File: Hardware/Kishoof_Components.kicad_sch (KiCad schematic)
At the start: 54 parts, among them J1 SWD_Header, J2 Eurorack_10_pin_power, U1 STM32H7B0VBTx, U2 PCM5100APW, U3 TPS561201, U4 LT1117-3.3, U5 TL074, U6 MX25LM51245G, Y1 8MHz 20pF

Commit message: Additional schematic layout
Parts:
- added C33, C34: 100nF, Capacitor_SMD:C_0603_1608Metric_Pad1.08x0.95mm_HandSolder, symbol Device:C_Small
- added C35: 1.5nF, Capacitors_SMD:C_0603_HandSoldering, symbol Device:C_Small
- added C36: 100nF, Capacitor_SMD:C_0603_1608Metric, symbol Device:C_Small
- added D3: LM4040DBZ-5, Package_TO_SOT_SMD:SOT-23, symbol Reference_Voltage:LM4040DBZ-10
- added J3, J4, J5, J6: Conn_01x08_Pin, Connector_PinHeader_2.54mm:PinHeader_1x08_P2.54mm_Vertical, symbol Connector:Conn_01x08_Pin
- added R11, R16, R18: 75k, Resistor_SMD:R_0603_1608Metric_Pad0.98x0.95mm_HandSolder, symbol Device:R
- added R12, R17, R20: 91k, Resistor_SMD:R_0603_1608Metric_Pad0.98x0.95mm_HandSolder, symbol Device:R
- added R13: 47k, Resistors_SMD:R_0603_HandSoldering, symbol Device:R
- added R14: 2k2, Resistor_SMD:R_0603_1608Metric_Pad0.98x0.95mm_HandSolder, symbol Device:R_Small
- added R15: 22, Resistor_SMD:R_0603_1608Metric_Pad0.98x0.95mm_HandSolder, symbol Device:R_Small
- added R19, R21: 47k, Resistor_SMD:R_0603_1608Metric_Pad0.98x0.95mm_HandSolder, symbol Device:R
- added U7, U8: MCP6004, Package_SO:SO-14_3.9x8.65mm_P1.27mm, symbol Amplifier_Operational:MCP6004
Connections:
- net +3.3V: now also R15.1
- net +3V3: now also U6.11 (VCC), U6.2 (VCC), C33.1, C34.1
- net -12V: now also R14.1
- net AUDIO_OUT_L: now also J4.1 (Pin_1)
- net AUDIO_OUT_R: now also J4.2 (Pin_2)
- net GND: now also U6.10 (GND), U6.6 (GND), C33.2, C34.2, C36.1, D3.1 (K), U7.3 (+), U7.5 (+), U8.3 (+)
- net OCTOSPIM_P1_DQS: no longer U1.23 (PA1)
- net OCTOSPIM_P1_IO0: no longer U1.18 (PC3_C), U1.58 (PD11)
- net OCTOSPIM_P1_IO1: no longer U1.34 (PB0)
- net OCTOSPIM_P1_IO2: no longer U1.1 (PE2)
- net OCTOSPIM_P1_IO3: no longer U1.30 (PA6)
- net OCTOSPIM_P1_IO4: no longer U1.85 (PD4)
- net OCTOSPIM_P1_IO5: no longer U1.86 (PD5)
- net OCTOSPIM_P1_IO6: no longer U1.87 (PD6)
- net OCTOSPIM_P1_IO7: no longer U1.88 (PD7)
- net OCTOSPIM_P1_NCS: now also U1.41 (PE11)
- net WAVETABLE_POS_A_POT: now reaches U1.22 (PA0)
- net WAVETABLE_POS_A_POT: now also J4.4 (Pin_4)
- net Pitch_CV_Scaled: now reaches U1.24 (PA2)
- net Pitch_CV_Scaled: now also C35.1, R13.1, U7.7
- net WaveTable_Pos_A_CV: now reaches U1.25 (PA3)
- net WaveTable_Pos_A_CV: now also R19.1, U7.1
- net WaveTable_Pos_B_CV: now reaches U1.28 (PA4)
- net WaveTable_Pos_B_CV: now also R21.1, U8.1
- net LCD_DC: now reaches U1.8 (PC14)
- net LCD_DC: now also J3.3 (Pin_3)
- net LCD_RESET: now reaches U1.9 (PC15)
- net LCD_RESET: now also J3.4 (Pin_4)
- net DAC_OUT_L renamed DAC_Out_L
- net DAC_OUT_R renamed DAC_Out_R
- net SPI3_MOSI renamed LCD_SPI3_MOSI
- net LCD_SPI3_MOSI: now also J3.2 (Pin_2)
- net SPI3_SCK renamed LCD_SPI3_SCK
- net LCD_SPI3_SCK: now also J3.1 (Pin_1)
- new net: R11.1, R12.1, R21.2, U8.2 (-)
- new net: R16.1, R17.1, R19.2, U7.2 (-)
- new net: C35.2, R13.2, R18.1, R20.1, U7.6 (-)
- new net -5V_REF: C36.2, D3.2 (A), R11.2, R14.2, R16.2, R18.2
- new net LCD_BACKLIGHT: J3.5 (Pin_5), R15.2
- new net PITCH_CV: J4.3 (Pin_3), R20.2
- new net WAVETABLE_POS_A_CV: J4.7 (Pin_7), R17.2
- new net WAVETABLE_POS_B_CV: J4.8 (Pin_8), R12.2
- new net WAVETABLE_POS_B_POT: J4.5 (Pin_5), U1.23 (PA1)
- no-connect marks 0 -> 1
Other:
- note added: "(-5*-47/75) + (cv*-47/91): 0V > 3.13V; 6V > 0.034V"
- note added: "22ohms gives 150mA"
- moved on the sheet: C1, C10, C11, C12, C13, C2, C25, C26, C27, C28, C29, C30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

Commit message: Implemented basic stepped mode for separate wavetables on A and B
Inverted waveform on display
Updates to hardware design
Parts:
- removed U5: TL074, Package_SO:SOIC-14_3.9x8.7mm_P1.27mm, symbol Amplifier_Operational:TL074
- added JP1: Jumper, Jumper:SolderJumper-2_P1.3mm_Open_RoundedPad1.0x1.5mm, symbol Jumper:Jumper_2_Open
- added unit 5 of U7
- added U8: TL072, Package_SO:SOIC-8_3.9x4.9mm_P1.27mm, symbol Amplifier_Operational:TL072
- added U9: STF202-22T1G, Custom_Footprints:STF202-22T1G, symbol STF202-22T1G:STF202-22T1G
- C10, C11, C13, C25, C26, C27, C29, C30, C31, C32, C33, C34: footprint Capacitor_SMD:C_0603_1608Metric_Pad1.08x0.95mm_HandSolder -> Capacitor_SMD:C_0603_1608Metric
- C14, C15, C35: footprint Capacitors_SMD:C_0603_HandSoldering -> Capacitor_SMD:C_0603_1608Metric
- C8: footprint Capacitor_SMD:C_0805_2012Metric -> Capacitor_SMD:C_0603_1608Metric
- R1, R10, R11, R12, R14, R15, R16, R17, R18, R19, R2, R20, R21, R3, R4, R5, R6, R7, R8, R9: footprint Resistor_SMD:R_0603_1608Metric_Pad0.98x0.95mm_HandSolder -> Resistor_SMD:R_0603_1608Metric
- R13: footprint Resistors_SMD:R_0603_HandSoldering -> Resistor_SMD:R_0603_1608Metric
- U7: footprint SMD_Packages:SOIC-14_N -> Package_SO:SO-14_3.9x8.65mm_P1.27mm; Part_Number C7378 -> C116668
- renumbered U8 to U7
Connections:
- net +12V: now also U8.8 (V+)
- net +3.3VA: now also U7.4 (V+)
- net -12V: now also U8.4 (V-)
- net GND: now also U7.10 (+), U7.11 (V-), U8.2 (-), U8.6 (-), U9.6 (GND); no longer U7.3 (+)
- net USB_DM: now also U9.2 (D1_OUT)
- net USB_DP: now also U9.3 (D2_OUT)
- net USB_VBUS: now also J5.6 (Pin_6)
- net WaveTable_Pos_B_CV: now also U7.8; no longer U7.1
- net at C32.1, R10.1, R8.1: now also U8.7
- net at C32.2, R6.1, R8.2: now also U8.5 (+)
- net at R11.1, R12.1, R21.2: now also U7.9 (-); no longer U7.2 (-)
- net at C31.2, R5.1, R7.2: now also U8.3 (+)
- net ADC6: now reaches U1.15 (PC0)
- net ADC7: now reaches U1.16 (PC1)
- net ADC1: now reaches U1.29 (PA5)
- net ADC2: now reaches U1.30 (PA6)
- net ADC3: now reaches U1.31 (PA7)
- net ADC4: now reaches U1.34 (PB0)
- net ADC5: now reaches U1.35 (PB1)
- net ENCODER_UP: now reaches U1.63 (PC6)
- net ENCODER_UP: now also J5.1 (Pin_1)
- net ENCODER_DN: now reaches U1.64 (PC7)
- net ENCODER_DN: now also J5.2 (Pin_2)
- net ENCODER_BTN: now reaches U1.65 (PC8)
- net ENCODER_BTN: now also J5.3 (Pin_3)
- net at C31.1, R7.1, R9.1: now also U8.1
- net USB_D+: now reaches J5.7 (Pin_7)
- net USB_D+: now also U9.4 (D2_IN)
- net USB_D-: now reaches J5.8 (Pin_8)
- net USB_D-: now also U9.5 (D1_IN)
- new net: JP1.1 (A), U9.1 (VBUS)
- new net VBUS: JP1.2 (B)

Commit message: Implemented basic 10 harmonic additive wave for channel B in smooth mode
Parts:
- added R22: 75k, Resistor_SMD:R_0603_1608Metric, symbol Device:R
- added R23: 91k, Resistor_SMD:R_0603_1608Metric, symbol Device:R
- added R24: 47k, Resistor_SMD:R_0603_1608Metric, symbol Device:R
- added U5: MCP6004, Package_SO:SO-14_3.9x8.65mm_P1.27mm, symbol Amplifier_Operational:MCP6004
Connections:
- net ADC2 is gone; now on net WARP_POT: U1.30 (PA6)
- net -5V_REF: now also R22.2
- net GND: now also U5.10 (+)
- net WARP_POT: now reaches J6.1 (Pin_1)
- net WARP_CV: now reaches J6.2 (Pin_2)
- net WARP_CV: now also R23.2
- net ADC1 renamed Warp_CV
- net Warp_CV: now also R24.1, U5.8
- new net: R22.1, R23.1, R24.2, U5.9 (-)
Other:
- moved on the sheet: C35, R11, R12, R13, R16, R17, R18, R19, R20, R21, U7A, U7B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

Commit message: Rearranged Panel
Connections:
- net WARP_BIPOLAR: now reaches U1.44 (PE14)
- net WARP_BIPOLAR: now also J6.3 (Pin_3)
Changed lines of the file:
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@@
+		)
+	)
+	(label "WARP_BIPOLAR"
+		(at 81.28 104.14 180)
+		(fields_autoplaced yes)
+		(effects
+			(font
+				(size 1.27 1.27)
+			)
+			(justify right bottom)
 		)
 	)
@@
 		(fields_autoplaced yes)
 		(effects
+			(font
+				(size 1.27 1.27)
+			)
+			(justify left bottom)
+		)
+	)
+	(label "WARP_BIPOLAR"
+		(at 480.06 199.39 0)
+		(fields_autoplaced yes)
+		(effects

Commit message: Updating component and panel PCBs
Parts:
- removed J3, J4, J5, J6: Conn_01x08_Pin, Connector_PinHeader_2.54mm:PinHeader_1x08_P2.54mm_Vertical, symbol Connector:Conn_01x08_Pin
- added J10: VOct, Custom_Footprints:THONKICONN_hole, symbol thonkiconn:AudioJack2_Ground_Switch
- added J11: WavetablePosA, Custom_Footprints:THONKICONN_hole, symbol thonkiconn:AudioJack2_Ground_Switch
- added J12: WavetablePos, Custom_Footprints:THONKICONN_hole, symbol thonkiconn:AudioJack2_Ground_Switch
- added J13: VCA, Custom_Footprints:THONKICONN_hole, symbol thonkiconn:AudioJack2_Ground_Switch
- added J14, J15, J16, J17: Conn_01x02_Socket, Connector_PinSocket_2.54mm:PinSocket_1x02_P2.54mm_Vertical, symbol Connector:Conn_01x02_Socket
- added J18: USB_C_Receptacle, Custom_Footprints:USB_C_Receptacle_Amphenol_12401951E412A, symbol Connector:USB_C_Receptacle
- added J7: Audio_Out_L, Custom_Footprints:THONKICONN_hole, symbol thonkiconn:AudioJack2_Ground_Switch
- added J8: Audio_Out_R, Custom_Footprints:THONKICONN_hole, symbol thonkiconn:AudioJack2_Ground_Switch
- added J9: WarpCV, Custom_Footprints:THONKICONN_hole, symbol thonkiconn:AudioJack2_Ground_Switch
- added R25: 75k, Resistor_SMD:R_0603_1608Metric, symbol Device:R
- added R26: 91k, Resistor_SMD:R_0603_1608Metric, symbol Device:R
- added R27: 47k, Resistor_SMD:R_0603_1608Metric, symbol Device:R
- added R28, R29: 5k1, Resistor_SMD:R_0805_2012Metric, symbol Device:R_Small
- added R30, R31: 10k, Resistor_SMD:R_0603_1608Metric, symbol Device:R_Small
- added RV1: WarpTypePot, Custom_Footprints:Bourns_Switch_Potentiometer, symbol Mountjoy:Switch_Potentiometer
- added SW1: Encoder, Custom_Footprints:Encoder, symbol Device:RotaryEncoder_Switch
- added SW2: Mode_Switch, Custom_Footprints:SPDT_Miniature, symbol Switch:SW_SPDT
- added SW3: Octave_Switch, Custom_Footprints:SP3T_Mini_Switch, symbol Switch:SW_SPDT_MSM
- added SW4: ChB_Output, Custom_Footprints:SP3T_Mini_Switch, symbol Switch:SW_SPDT_MSM
- added SW5: SW_Push, Custom_Footprints:SW_PUSH_6mm_aligned, symbol Switch:SW_Push
- added TP1: TestPoint, TestPoint:TestPoint_Pad_D1.0mm, symbol Connector:TestPoint
- added U5: MCP6002, Package_SO:SOIC-8_3.9x4.9mm_P1.27mm, symbol Amplifier_Operational:MCP6002-xSN
- added WarpAmtPot1, WaveTablePot1, WaveTablePot2: B10k, Custom_Footprints:Alpha_9mm_Potentiometer_Aligned, symbol Device:R_Potentiometer
- C9: footprint Resistor_SMD:R_1206_3216Metric -> Capacitor_SMD:C_1206_3216Metric
- U2: footprint Custom_Footprints:SSOP-20_4.4x6.5mm_Pitch0.65mm_Round_Pads -> Package_SO:TSSOP-20_4.4x6.5mm_P0.65mm
- U3: footprint Package_TO_SOT_SMD:SOT-23-6_Handsoldering -> TO_SOT_Packages_SMD:SOT-23-6_Handsoldering
- renumbered U5 to U7
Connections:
- net +3.3V: now also J17.1 (Pin_1), R30.2, SW2.1 (A), SW3.2 (3), SW4.2 (3)
- net +3.3VA: now also RV1.1, U5.8 (V+), WarpAmtPot1.1, WaveTablePot1.1, WaveTablePot2.1
- net -5V_REF: now also R25.2
- net AUDIO_OUT_L: now also J7.3
- net AUDIO_OUT_R: now also J8.3
- net ENCODER_BTN: now also SW1.S1
- net ENCODER_DN: now also SW1.B
- net ENCODER_UP: now also SW1.A
- net GND: now also U7.12 (+), J10.1, J10.2, J11.1, J11.2, J12.1, J12.2, J13.1, J13.2, J17.2 (Pin_2), J18.A1 (GND), J18.A12 (GND), J18.B1 (GND), J18.B12 (GND), J18.S1 (SHIELD), J7.1, J8.1, J9.1, J9.2, R28.2, R29.2, R31.1, RV1.3, RV1.4 (1), SW1.C, SW1.S2, SW2.3 (C), SW5.2, U5.3 (+), U5.4 (V-), WarpAmtPot1.3, WaveTablePot1.3, WaveTablePot2.3; no longer U7.10 (+)
- net LCD_BACKLIGHT: now also J16.1 (Pin_1)
- net LCD_DC: now also J15.1 (Pin_1)
- net LCD_RESET: now also J15.2 (Pin_2)
- net LCD_SPI3_MOSI: now also J14.2 (Pin_2)
- net LCD_SPI3_SCK: now also J14.1 (Pin_1)
- net PITCH_CV: now also J10.3
- net RESET: now also TP1.1
- net USB_D+: now also J18.A6 (D+), J18.B6 (D+)
- net USB_D-: now also J18.A7 (D-), J18.B7 (D-)
- net VBUS: now also J18.A4 (VBUS), J18.A9 (VBUS), J18.B4 (VBUS), J18.B9 (VBUS)
- net WARP_CV: now also J9.3
- net WAVETABLE_POS_A_CV: now also J11.3
- net WAVETABLE_POS_A_POT: now also WaveTablePot2.2
- net WAVETABLE_POS_B_CV: now also J12.3
- net WAVETABLE_POS_B_POT: now also WaveTablePot1.2
- net at R22.1, R23.1, R24.2: now also U7.13 (-); no longer U7.9 (-)
- net ChB_Mix: now reaches U1.42 (PE12)
- net ChB_Mix: now also SW4.1
- net ChB_RM: now reaches U1.43 (PE13)
- net ChB_RM: now also SW4.3 (4)
- net Mode: now reaches U1.45 (PE15)
- net Mode: now also SW2.2 (B)
- net B_Octave_Btn1: now reaches U1.62 (PD15)
- net B_Octave_Btn1: now also SW5.1
- net LCD_SPI3_SS: now reaches U1.77 (PA15)
- net LCD_SPI3_SS: now also J16.2 (Pin_2)
- net Octave_Up: now reaches U1.81 (PD0)
- net Octave_Up: now also SW3.1
- net Octave_Down: now reaches U1.82 (PD1)
- net Octave_Down: now also SW3.3 (4)
- net Warp_Polarity_Btn: now reaches U1.92 (PB6)
- net Warp_Polarity_Btn: now also RV1.5 (2)
- net ADC3 renamed VcaCV
- net VcaCV: now also R27.1, U5.1
- net ADC4 renamed Warp_Type_Pot
- net Warp_Type_Pot: now also RV1.2
- net ADC5: no longer names the net of U1.35 (PB1)
- net ADC6: no longer names the net of U1.15 (PC0)
- net ADC7: no longer names the net of U1.16 (PC1)
- net WARP_POT renamed WARP_AMT_POT
- net WARP_AMT_POT: now also WarpAmtPot1.2
- net Warp_CV renamed WarpCV
- net WarpCV: now also U7.14; no longer U7.8
- net WaveTable_Pos_A_CV renamed WavetablePosA_CV
- net WaveTable_Pos_B_CV renamed WavetablePosB_CV
- new net: J18.A5 (CC1), R28.1
- new net: J18.B5 (CC2), R29.1
- new net: R25.1, R26.1, R27.2, U5.2 (-)
- new net: R30.1, R31.2, U5.5 (+)
- new net: U5.6 (-), U5.7
- new net VCA_CV: J13.3, R26.2
- no-connect marks 1 -> 21
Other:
- note added: "OCTOSPIM_P1_IO0"
- note added: "OCTOSPIM_P1_IO4"
- note added: "OCTOSPIM_P1_IO5"
- note added: "OCTOSPIM_P1_IO6"
- note added: "OCTOSPIM_P1_IO7"
- note added: "SPARE_ADC"
- moved on the sheet: U7E

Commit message: Schematic updates
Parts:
- added WarpAmtTrm2, WavetableATrm1: B10k, Custom_Footprints:Alpha_9mm_Potentiometer_Aligned, symbol Device:R_Potentiometer
- C12, C28: footprint Capacitor_SMD:C_0805_2012Metric -> Capacitor_SMD:C_0603_1608Metric
- Y1: footprint Crystals:Crystal_SMD_5032-2pin_5.0x3.2mm_HandSoldering -> Crystal:Crystal_SMD_Abracon_ABM3-2Pin_5.0x3.2mm
- renumbered RV1 to WarpType1, WaveTablePot2 to WavetableAPot1, WaveTablePot1 to WavetableBPot1
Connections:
- net +3.3VA: now also WarpAmtTrm2.1, WavetableATrm1.1
- net GND: now also WarpAmtTrm2.3, WavetableATrm1.3
- net OCTOSPIM_P1_NCS: no longer U1.46 (PB10)
- net WARP_AMT_TRM: now reaches U1.15 (PC0)
- net WARP_AMT_TRM: now also WarpAmtTrm2.2
- net WAVETABLE_POS_A_TRM: now reaches U1.16 (PC1)
- net WAVETABLE_POS_A_TRM: now also WavetableATrm1.2
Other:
- note added: "OCTOSPIM_P1_NCS"
- moved on the sheet: WavetableBPot1

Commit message: First draft signal routing on component pcb
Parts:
- removed R30, R31: 10k, Resistor_SMD:R_0603_1608Metric, symbol Device:R_Small
- added C37: 2.2nF, Capacitor_SMD:C_0603_1608Metric, symbol Device:C_Small
- added C38, C39: 2.2uF, Capacitor_SMD:C_0603_1608Metric, symbol Device:C_Small
- added J4: Conn_01x01_Socket, Connector_PinSocket_2.54mm:PinSocket_1x01_P2.54mm_Vertical, symbol Connector:Conn_01x01_Socket
- added R32: 20k, Resistor_SMD:R_0603_1608Metric, symbol Device:R
- added R33: 47k, Resistor_SMD:R_0603_1608Metric, symbol Device:R
- added R34: 6k8, Resistor_SMD:R_0603_1608Metric, symbol Device:R
- C29, C30: value 2n2 -> 2.2nF
- C35: value 1.5nF -> 2.2nF
- R28, R29: footprint Resistor_SMD:R_0805_2012Metric -> Resistor_SMD:R_0603_1608Metric
- U3: footprint TO_SOT_Packages_SMD:SOT-23-6_Handsoldering -> Package_TO_SOT_SMD:TSOT-23-6_HandSoldering
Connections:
- net +3V3 is gone; now on net +3.3V: C13.1, C28.1, C33.1, C34.1, U2.17 (XSMT), U2.20 (DVDD), U6.11 (VCC), U6.2 (VCC)
- net VBUS is gone; now on net USB_VBUS: J18.A4 (VBUS), J18.A9 (VBUS), J18.B4 (VBUS), J18.B9 (VBUS), JP1.2 (B)
- net -5V_REF: now also R32.2
- net GND: now also J16.2 (Pin_2), U5.6 (-), C38.2, C39.2; no longer J17.2 (Pin_2)
- net LCD_BACKLIGHT: now also J17.2 (Pin_2); no longer J16.1 (Pin_1)
- net LCD_DC: now also U1.92 (PB6); no longer U1.8 (PC14)
- net LCD_RESET: now also U1.93 (PB7); no longer U1.9 (PC15)
- net LCD_SPI3_MOSI: now also J14.1 (Pin_1); no longer J14.2 (Pin_2)
- net LCD_SPI3_SCK: now also J14.2 (Pin_2); no longer J14.1 (Pin_1)
- net LCD_SPI3_SS: now also J16.1 (Pin_1); no longer J16.2 (Pin_2)
- net Mode: now also U1.1 (PE2); no longer U1.45 (PE15)
- net PITCH_CV: now also R23.2; no longer R20.2
- net Pitch_CV_Scaled: now also R24.1, U1.28 (PA4), U5.7; no longer R13.1, U1.24 (PA2), U7.7
- net VcaCV: now also U7.14; no longer U5.1
- net WARP_AMT_POT: now also U1.16 (PC1); no longer U1.30 (PA6)
- net WARP_CV: now also R20.2; no longer R23.2
- net WAVETABLE_POS_A_POT: now also U1.30 (PA6); no longer U1.22 (PA0)
- net WAVETABLE_POS_A_TRM: now also U1.23 (PA1); no longer U1.16 (PC1)
- net WAVETABLE_POS_B_POT: now also U1.22 (PA0); no longer U1.23 (PA1)
- net WarpCV: now also R13.1, U1.25 (PA3), U7.7; no longer R24.1, U1.29 (PA5), U7.14
- net Warp_Polarity_Btn: now also U1.2 (PE3); no longer U1.92 (PB6)
- net WavetablePosA_CV: now also U1.35 (PB1), U5.1; no longer U1.25 (PA3), U7.1
- net WavetablePosB_CV: now also U1.29 (PA5); no longer U1.28 (PA4)
- net at R22.1, R23.1, R24.2: now also C35.2, U5.5 (+); no longer U7.13 (-)
- net at R25.1, R26.1, R27.2: now also U7.13 (-); no longer U5.2 (-)
- net at R16.1, R17.1, R19.2: now also U5.2 (-); no longer U7.2 (-)
- net at R13.2, R18.1, R20.1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: no longer C35.2
- net at U1.48 (VCAP): now also C38.1
- net at U1.73 (VCAP): now also C39.1
- net WARP_BIPOLAR: no longer names the net of U1.44 (PE14)
- new net: C37.2, R32.1, R33.1, R34.2, U7.2 (-)
- new net AudioIn: C37.1, R34.1, U1.24 (PA2), U7.1
- new net EXT_AUDIO_IN: J4.1 (Pin_1), R33.2
- no-connect marks 21 -> 47
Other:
- note removed: "OCTOSPIM_P1_IO0"
- note removed: "OCTOSPIM_P1_IO4"
- note removed: "OCTOSPIM_P1_IO5"
- note removed: "OCTOSPIM_P1_IO6"
- note removed: "OCTOSPIM_P1_IO7"
- note removed: "OCTOSPIM_P1_NCS"
- note removed: "SPARE_ADC"
- moved on the sheet: C10, C11, C12, C13, C14, C15, C16, C17, C18, C19, C20, C21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

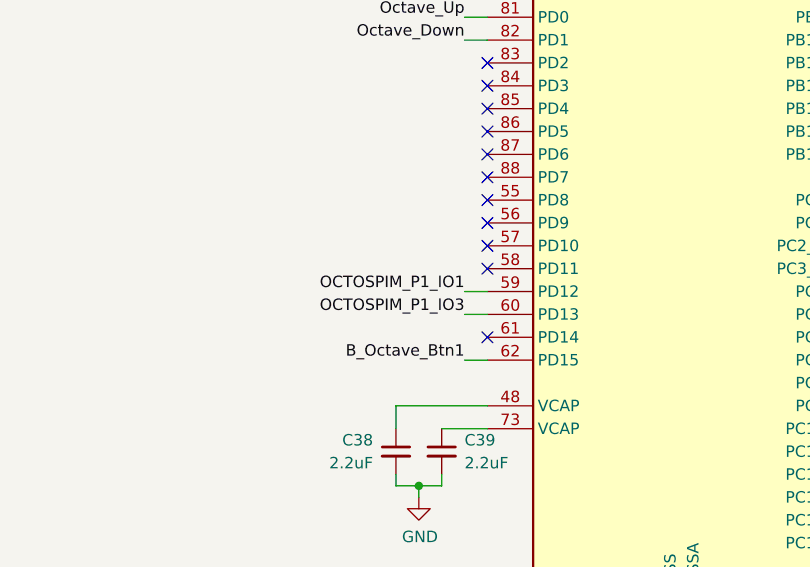
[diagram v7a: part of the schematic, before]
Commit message: Started routing power
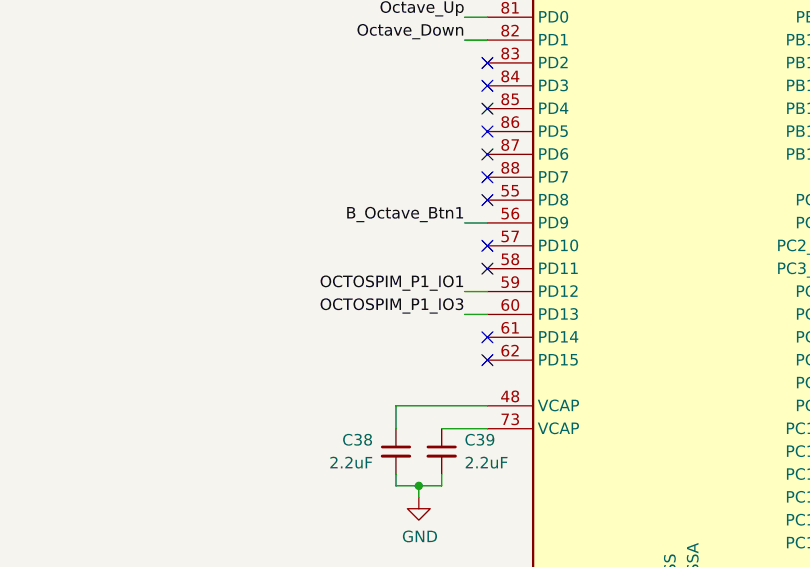
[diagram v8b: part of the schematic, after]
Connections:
- net B_Octave_Btn1: now also U1.56 (PD9); no longer U1.62 (PD15)
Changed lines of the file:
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@@
 	)
 	(no_connect
-		(at 69.85 135.89)
+		(at 69.85 151.13)
 	)
 	(no_connect
@@
 	(wire
 		(pts
-			(xy 67.31 151.13) (xy 69.85 151.13)
+			(xy 67.31 135.89) (xy 69.85 135.89)
 		)
 		(stroke
@@
 	)
 	(label "B_Octave_Btn1"
-		(at 67.31 151.13 180)
+		(at 67.31 135.89 180)
 		(fields_autoplaced yes)
 		(effects
